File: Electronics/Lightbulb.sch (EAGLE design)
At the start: 22 parts, among them IC2 7805L

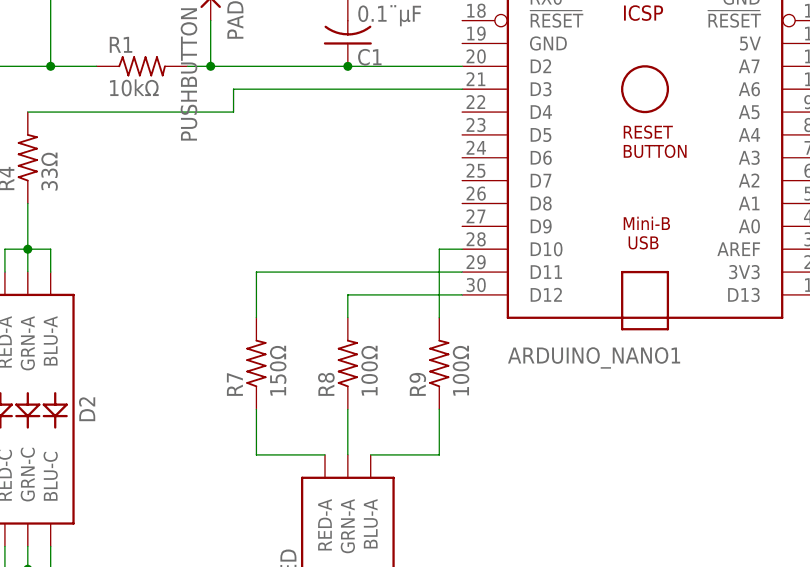
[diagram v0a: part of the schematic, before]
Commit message: Moving switches and LEDs to bottom side of board
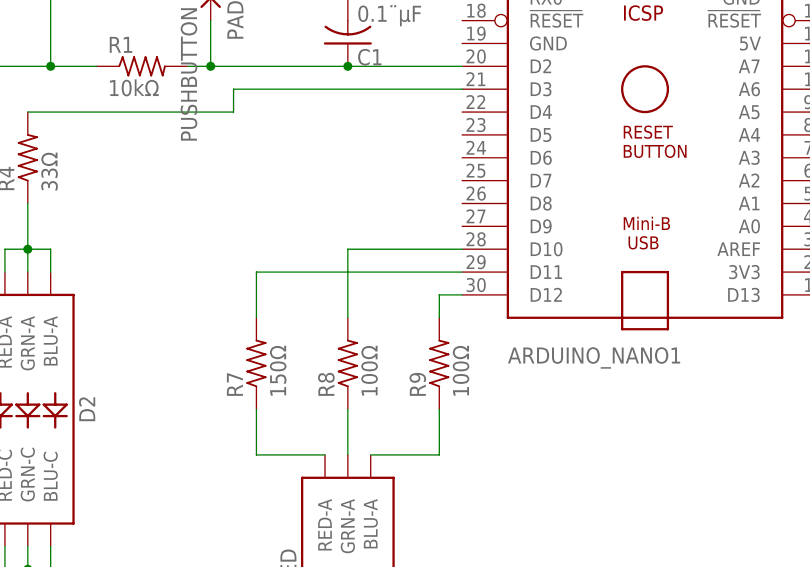
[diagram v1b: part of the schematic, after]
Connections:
- net N$12: now also ARDUINO_NANO1.D10; no longer ARDUINO_NANO1.D12
- net N$2: now also ARDUINO_NANO1.D12; no longer ARDUINO_NANO1.D10
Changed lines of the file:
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@@
-</segment>
-</net>
-<net name="N$2" class="0">
-<segment>
-<pinref part="R9" gate="G$1" pin="2"/>
-<wire x1="96.52" y1="58.42" x2="96.52" y2="66.04" width="0.1524" layer="91"/>
-<pinref part="ARDUINO_NANO1" gate="G$1" pin="D10"/>
-<wire x1="96.52" y1="66.04" x2="99.06" y2="66.04" width="0.1524" layer="91"/>
 </segment>
 </net>
@@
 </segment>
 </net>
-<net name="N$12" class="0">
-<segment>
-<pinref part="R8" gate="G$1" pin="2"/>
-<wire x1="86.36" y1="58.42" x2="86.36" y2="60.96" width="0.1524" layer="91"/>
-<pinref part="ARDUINO_NANO1" gate="G$1" pin="D12"/>
-<wire x1="86.36" y1="60.96" x2="99.06" y2="60.96" width="0.1524" layer="91"/>
-</segment>
-</net>
 <net name="N$1" class="0">
 <segment>
@@
 </segment>
 </net>
+<net name="N$2" class="0">
+<segment>
+<pinref part="ARDUINO_NANO1" gate="G$1" pin="D12"/>
+<wire x1="99.06" y1="60.96" x2="96.52" y2="60.96" width="0.1524" layer="91"/>
+<pinref part="R9" gate="G$1" pin="2"/>
+<wire x1="96.52" y1="60.96" x2="96.52" y2="58.42" width="0.1524" layer="91"/>
+</segment>
+</net>
+<net name="N$12" class="0">
+<segment>
+<pinref part="R8" gate="G$1" pin="2"/>
+<wire x1="86.36" y1="58.42" x2="86.36" y2="66.04" width="0.1524" layer="91"/>
+<pinref part="ARDUINO_NANO1" gate="G$1" pin="D10"/>
+<wire x1="86.36" y1="66.04" x2="99.06" y2="66.04" width="0.1524" layer="91"/>
+</segment>
+</net>

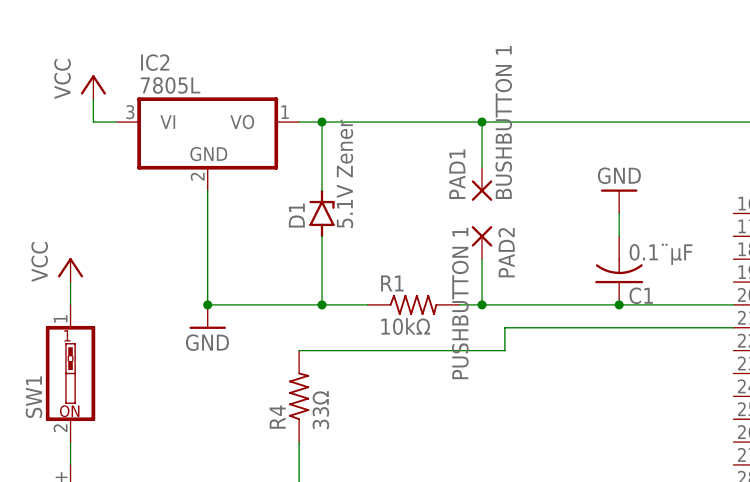
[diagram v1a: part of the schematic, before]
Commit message: Correcting pad placement and connections on PCB
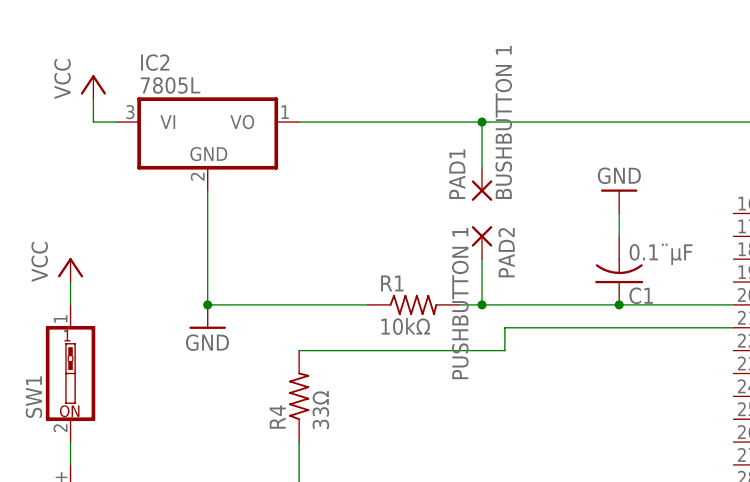
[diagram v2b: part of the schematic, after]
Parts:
- removed D1: 5.1V Zener, diode:ZENER-DIODESOD64-12
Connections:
- net GND: no longer D1.A
- net N$4: no longer D1.C
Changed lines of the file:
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@@
 <setting verticaltext="up"/>
 </settings>
-<grid distance="0.1" unitdist="inch" unit="inch" style="lines" multiple="1" display="yes" altdistance="0.01" altunitdist="inch" altunit="inch"/>
+<grid distance="0.1" unitdist="inch" unit="inch" style="lines" multiple="1" display="no" altdistance="0.01" altunitdist="inch" altunit="inch"/>
 <layers>
 <layer number="1" name="Top" color="4" fill="1" visible="no" active="no"/>
@@
 <part name="GND8" library="supply1" library_urn="urn:adsk.eagle:library:371" deviceset="GND" device=""/>
 <part name="D4" library="diode" library_urn="urn:adsk.eagle:library:210" deviceset="ZENER-DIODE" device="SOD64-12" package3d_urn="urn:adsk.eagle:package:43356/1" value="5.1V Zener"/>
-<part name="D1" library="diode" library_urn="urn:adsk.eagle:library:210" deviceset="ZENER-DIODE" device="SOD64-12" package3d_urn="urn:adsk.eagle:package:43356/1" value="5.1V Zener"/>
 <part name="D2" library="SparkFun-LED" library_urn="urn:adsk.eagle:library:529" deviceset="LED-RGB" device="NO_IC" package3d_urn="urn:adsk.eagle:package:39374/1" value="WHITE LED"/>
 <part name="P+2" library="supply1" library_urn="urn:adsk.eagle:library:371" deviceset="VCC" device=""/>
@@
 <attribute name="VALUE" x="176.149" y="59.182" size="1.778" layer="96" rot="R90"/>
 </instance>
-<instance part="D1" gate="G$1" x="53.34" y="96.52" rot="R90">
-<attribute name="NAME" x="51.435" y="94.742" size="1.778" layer="95" rot="R90"/>
-<attribute name="VALUE" x="56.769" y="94.742" size="1.778" layer="96" rot="R90"/>
-</instance>
 <instance part="D2" gate="G$1" x="50.8" y="48.26" rot="R270">
 <attribute name="NAME" x="56.515" y="48.26" size="1.778" layer="95" font="vector" rot="R270" align="bottom-center"/>
@@
 <net name="N$4" class="0">
 <segment>
-<wire x1="50.8" y1="106.68" x2="53.34" y2="106.68" width="0.1524" layer="91"/>
-<wire x1="53.34" y1="106.68" x2="71.12" y2="106.68" width="0.1524" layer="91"/>
+<wire x1="50.8" y1="106.68" x2="71.12" y2="106.68" width="0.1524" layer="91"/>
 <wire x1="71.12" y1="106.68" x2="71.12" y2="101.6" width="0.1524" layer="91"/>
 <wire x1="71.12" y1="106.68" x2="152.4" y2="106.68" width="0.1524" layer="91"/>
 <junction x="71.12" y="106.68"/>
 <wire x1="152.4" y1="106.68" x2="152.4" y2="88.9" width="0.1524" layer="91"/>
-<wire x1="53.34" y1="99.06" x2="53.34" y2="106.68" width="0.1524" layer="91"/>
-<junction x="53.34" y="106.68"/>
 <pinref part="ARDUINO_NANO1" gate="G$1" pin="5V"/>
 <wire x1="139.7" y1="88.9" x2="144.78" y2="88.9" width="0.1524" layer="91"/>
@@
 <wire x1="144.78" y1="86.36" x2="144.78" y2="88.9" width="0.1524" layer="91"/>
 <junction x="144.78" y="88.9"/>
-<pinref part="D1" gate="G$1" pin="C"/>
 <pinref part="IC2" gate="A1" pin="VO"/>
 <pinref part="PAD1" gate="G$1" pin="P"/>
@@
 <segment>
 <pinref part="R1" gate="G$1" pin="1"/>
-<wire x1="58.42" y1="86.36" x2="53.34" y2="86.36" width="0.1524" layer="91"/>
-<wire x1="53.34" y1="86.36" x2="40.64" y2="86.36" width="0.1524" layer="91"/>
+<wire x1="58.42" y1="86.36" x2="40.64" y2="86.36" width="0.1524" layer="91"/>
 <wire x1="40.64" y1="99.06" x2="40.64" y2="86.36" width="0.1524" layer="91"/>
-<wire x1="53.34" y1="93.98" x2="53.34" y2="86.36" width="0.1524" layer="91"/>
-<junction x="53.34" y="86.36"/>
-<pinref part="D1" gate="G$1" pin="A"/>
 <pinref part="GND9" gate="1" pin="GND"/>
 <junction x="40.64" y="86.36"/>

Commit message: Updating board with custom-made footprints for push buttons
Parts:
- removed PAD1: BUSHBUTTON 1, wirepad:WIREPADSMD1,27-254
- removed PAD2: PUSHBUTTON 1, wirepad:WIREPADSMD1,27-254
- removed PAD3: BUSHBUTTON 2, wirepad:WIREPADSMD1,27-254
- removed PAD4: PUSHBUTTON 2, wirepad:WIREPADSMD1,27-254
- added U$1, U$2: SKRPABE010, Custom Library:SKRPABE010
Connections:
- net N$3: now also U$1.3, U$1.4; no longer PAD2.P
- net N$4: now also U$1.1, U$1.2; no longer PAD1.P
- net N$6: now also U$2.3, U$2.4; no longer PAD4.P
- net VCC: now also U$2.1, U$2.2; no longer PAD3.P

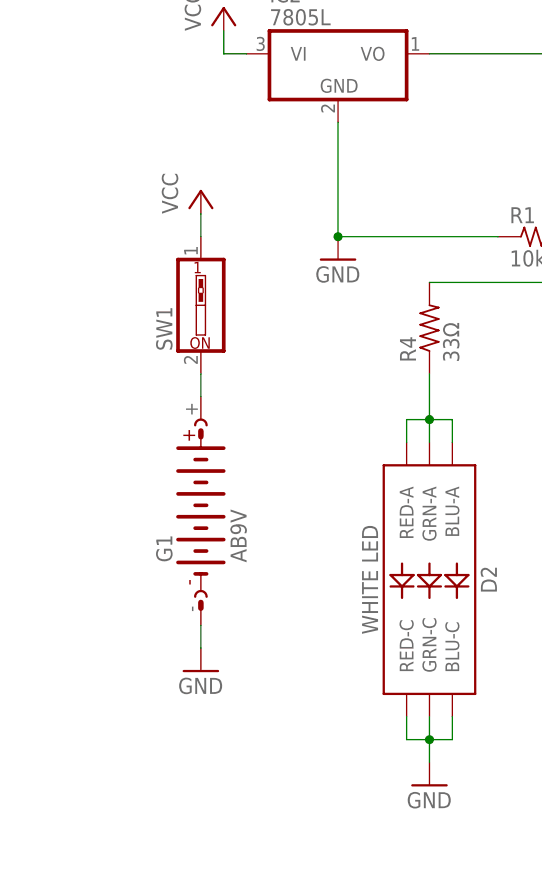
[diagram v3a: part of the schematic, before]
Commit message: Larger trace widths and new footprint for dip switch
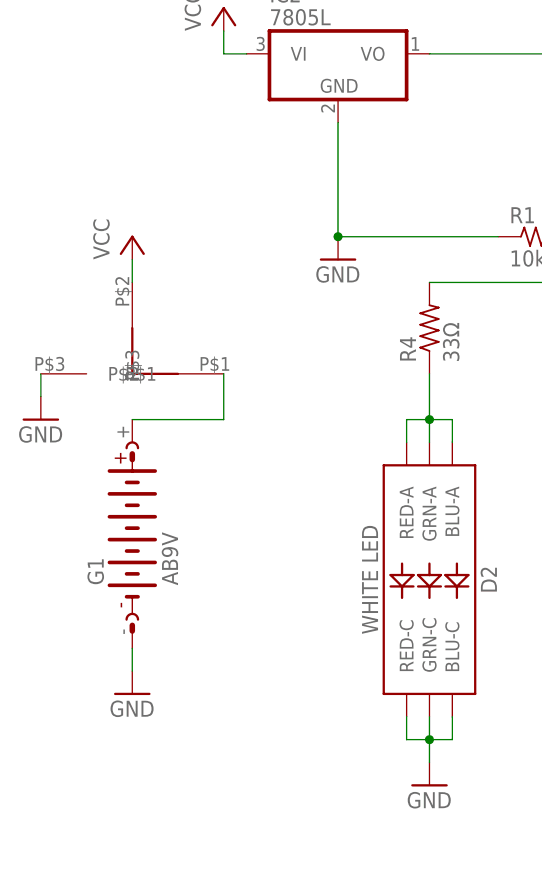
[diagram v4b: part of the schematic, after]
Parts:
- removed SW1: (no value), special:SW_DIP-1
- added U$3: DIPSWITCH, Custom Library:DIPSWITCH
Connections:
- net GND: now also U$3.P$2
- net N$1: now also U$3.P$1; no longer SW1.2
- net VCC: now also U$3.P$3; no longer SW1.1
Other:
- moved on the sheet: G1
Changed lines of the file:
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@@
 <setting verticaltext="up"/>
 </settings>
-<grid distance="0.1" unitdist="inch" unit="inch" style="lines" multiple="1" display="no" altdistance="0.01" altunitdist="mm" altunit="mm"/>
+<grid distance="0.1" unitdist="inch" unit="inch" style="lines" multiple="1" display="no" altdistance="0.01" altunitdist="inch" altunit="inch"/>
 <layers>
 <layer number="1" name="Top" color="4" fill="1" visible="yes" active="no"/>
@@
 </variantdefs>
 <classes>
-<class number="0" name="default" width="0.3048" drill="0.508">
+<class number="0" name="default" width="0.508" drill="0.508">
 <clearance class="0" value="0.3048"/>
 </class>
@@
 <part name="P+3" library="supply1" library_urn="urn:adsk.eagle:library:371" deviceset="VCC" device=""/>
 <part name="IC2" library="adafruit" deviceset="78*" device="L" technology="05"/>
-<part name="SW1" library="special" library_urn="urn:adsk.eagle:library:367" deviceset="SW_DIP-1" device="" package3d_urn="urn:adsk.eagle:package:26661/1"/>
 <part name="P+1" library="supply1" library_urn="urn:adsk.eagle:library:371" deviceset="VCC" device=""/>
 <part name="U$2" library="Custom Library" deviceset="SKRPABE010" device=""/>
 <part name="U$1" library="Custom Library" deviceset="SKRPABE010" device=""/>
+<part name="U$3" library="Custom Library" deviceset="DIPSWITCH" device=""/>
+<part name="GND10" library="supply1" library_urn="urn:adsk.eagle:library:371" deviceset="GND" device=""/>
 </parts>
 <sheets>
@@
 <attribute name="VALUE" x="145.796" y="79.629" size="1.778" layer="96"/>
 </instance>
-<instance part="G1" gate="G$1" x="25.4" y="55.88" rot="R90">
-<attribute name="NAME" x="22.225" y="50.165" size="1.778" layer="95" rot="R90"/>
-<attribute name="VALUE" x="30.48" y="50.165" size="1.778" layer="96" rot="R90"/>
+<instance part="G1" gate="G$1" x="17.78" y="53.34" rot="R90">
+<attribute name="NAME" x="14.605" y="47.625" size="1.778" layer="95" rot="R90"/>
+<attribute name="VALUE" x="22.86" y="47.625" size="1.778" layer="96" rot="R90"/>
 </instance>
 <instance part="GND1" gate="1" x="144.78" y="93.98" rot="R90">
 <attribute name="VALUE" x="147.32" y="91.44" size="1.778" layer="96" rot="R90"/>
 </instance>
-<instance part="GND2" gate="1" x="25.4" y="38.1">
-<attribute name="VALUE" x="22.86" y="35.56" size="1.778" layer="96"/>
+<instance part="GND2" gate="1" x="17.78" y="35.56">
+<attribute name="VALUE" x="15.24" y="33.02" size="1.778" layer="96"/>
 </instance>
 <instance part="ARDUINO_NANO1" gate="G$1" x="119.38" y="83.82">
@@
 <attribute name="VALUE" x="38.1" y="81.28" size="1.778" layer="96"/>
 </instance>
-<instance part="P+3" gate="VCC" x="25.4" y="91.44">
-<attribute name="VALUE" x="22.86" y="88.9" size="1.778" layer="96" rot="R90"/>
+<instance part="P+3" gate="VCC" x="17.78" y="86.36">
+<attribute name="VALUE" x="15.24" y="83.82" size="1.778" layer="96" rot="R90"/>
 </instance>
 <instance part="IC2" gate="A1" x="40.64" y="106.68">
@@
 <attribute name="VALUE" x="33.02" y="109.855" size="1.778" layer="96"/>
 </instance>
-<instance part="SW1" gate="G$1" x="25.4" y="78.74" rot="R90">
-<attribute name="NAME" x="22.225" y="73.66" size="1.778" layer="95" rot="R90"/>
-<attribute name="VALUE" x="30.48" y="73.66" size="1.778" layer="96" rot="R90"/>
-</instance>
 <instance part="P+1" gate="VCC" x="27.94" y="111.76">
 <attribute name="VALUE" x="25.4" y="109.22" size="1.778" layer="96" rot="R90"/>
@@
 <instance part="U$2" gate="G$1" x="165.1" y="99.06"/>
 <instance part="U$1" gate="G$1" x="76.2" y="101.6"/>
+<instance part="U$3" gate="G$1" x="17.78" y="71.12" rot="R180"/>
+<instance part="GND10" gate="1" x="7.62" y="66.04">
+<attribute name="VALUE" x="5.08" y="63.5" size="1.778" layer="96"/>
+</instance>
 </instances>
 <busses>
@@
 <pinref part="G1" gate="G$1" pin="-"/>
 <pinref part="GND2" gate="1" pin="GND"/>
-<wire x1="25.4" y1="40.64" x2="25.4" y2="43.18" width="0.1524" layer="91"/>
+<wire x1="17.78" y1="38.1" x2="17.78" y2="40.64" width="0.1524" layer="91"/>
 </segment>
 <segment>
@@
 <wire x1="88.9" y1="12.7" x2="88.9" y2="10.16" width="0.1524" layer="91"/>
 <wire x1="88.9" y1="10.16" x2="86.36" y2="10.16" width="0.1524" layer="91"/>
+</segment>
+<segment>
+<pinref part="U$3" gate="G$1" pin="P$2"/>
+<pinref part="GND10" gate="1" pin="GND"/>
+<wire x1="7.62" y1="68.58" x2="7.62" y2="71.12" width="0.1524" layer="91"/>
 </segment>
 </net>
@@
 </segment>
 <segment>
-<pinref part="SW1" gate="G$1" pin="1"/>
-<pinref part="P+3" gate="VCC" pin="VCC"/>
-<wire x1="25.4" y1="86.36" x2="25.4" y2="88.9" width="0.1524" layer="91"/>
-</segment>
-<segment>
 <pinref part="P+2" gate="VCC" pin="VCC"/>
 <wire x1="162.56" y1="106.68" x2="162.56" y2="104.14" width="0.1524" layer="91"/>
@@
 <wire x1="170.18" y1="99.06" x2="169.72" y2="99.06" width="0.1524" layer="91"/>
 </segment>
+<segment>
+<pinref part="U$3" gate="G$1" pin="P$3"/>
+<pinref part="P+3" gate="VCC" pin="VCC"/>
+<wire x1="17.78" y1="83.82" x2="17.78" y2="81.28" width="0.1524" layer="91"/>
+</segment>
 </net>
 <net name="N$8" class="0">
@@
 <pinref part="ARDUINO_NANO1" gate="G$1" pin="D11"/>
 <wire x1="76.2" y1="63.5" x2="99.06" y2="63.5" width="0.1524" layer="91"/>
-</segment>
-</net>
-<net name="N$1" class="0">
-<segment>
-<pinref part="G1" gate="G$1" pin="+"/>
-<pinref part="SW1" gate="G$1" pin="2"/>
-<wire x1="25.4" y1="68.58" x2="25.4" y2="71.12" width="0.1524" layer="91"/>
 </segment>
 </net>
@@
 </segment>
 </net>
+<net name="N$1" class="0">
+<segment>
+<pinref part="G1" gate="G$1" pin="+"/>
+<pinref part="U$3" gate="G$1" pin="P$1"/>
+<wire x1="17.78" y1="66.04" x2="27.94" y2="66.04" width="0.1524" layer="91"/>
+<wire x1="27.94" y1="66.04" x2="27.94" y2="71.12" width="0.1524" layer="91"/>
+</segment>
+</net>

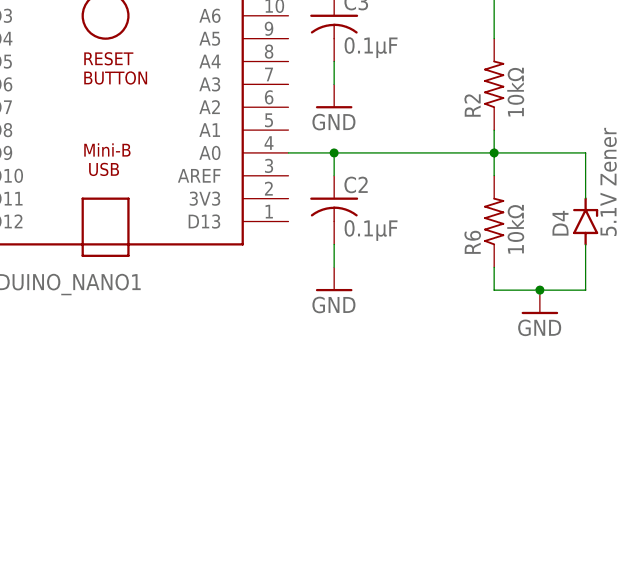
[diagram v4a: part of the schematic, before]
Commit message: Correct trace widths this time (Matt Brown approved)
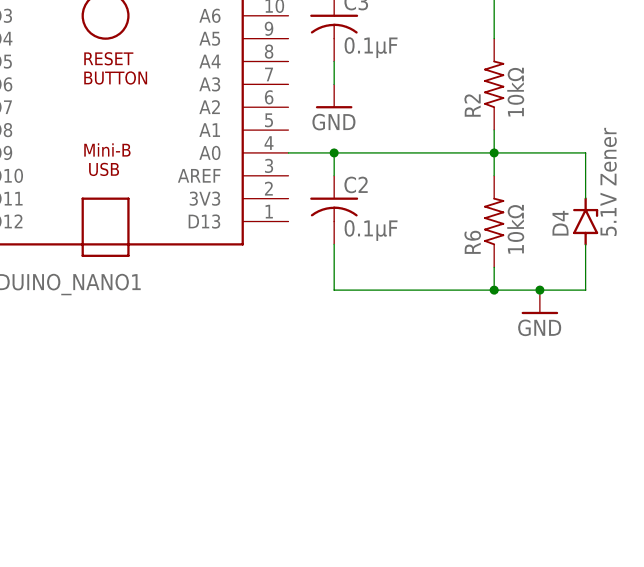
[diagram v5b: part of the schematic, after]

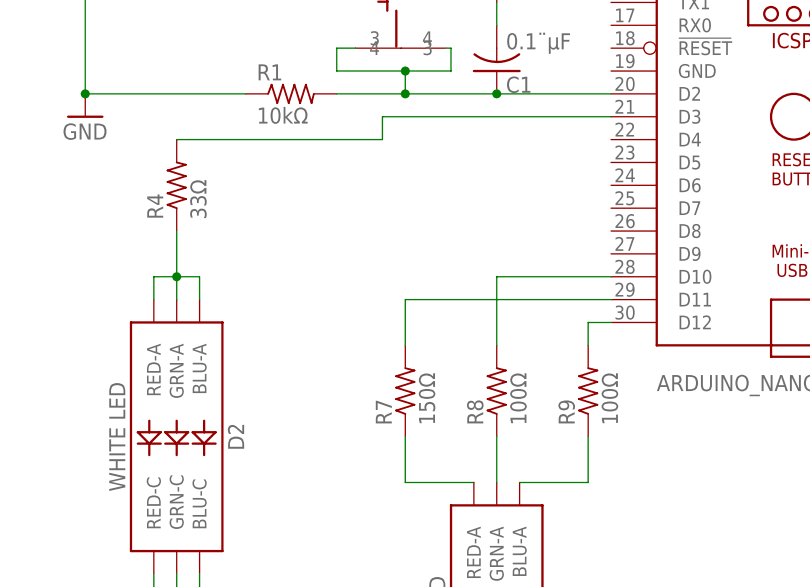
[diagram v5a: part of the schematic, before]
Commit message: updating a few resistor values for diodes to prevent draw of too much current from Arduino
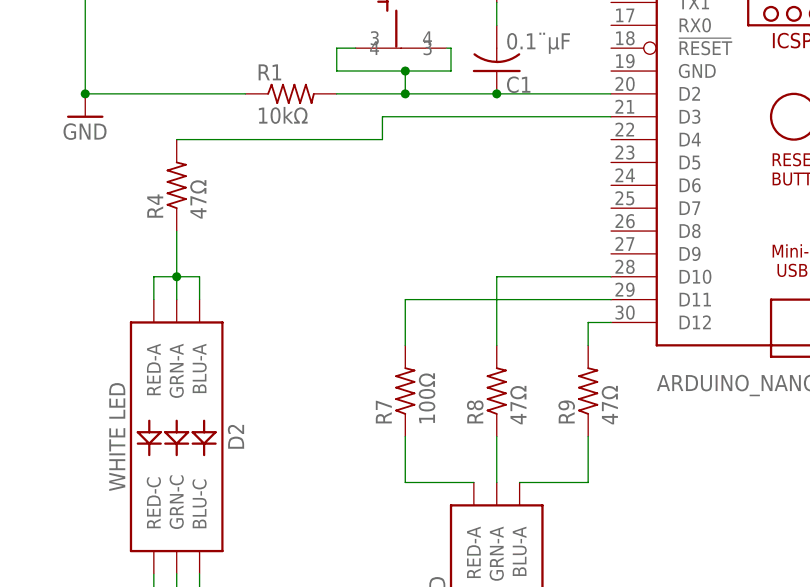
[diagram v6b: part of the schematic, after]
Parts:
- R4: value 33Ω -> 47Ω
- R7: value 150Ω -> 100Ω
- R8, R9: value 100Ω -> 47Ω
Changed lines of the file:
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@@
 <part name="R1" library="adafruit" deviceset="R-US_" device="R0805" value="10kΩ"/>
 <part name="R2" library="adafruit" deviceset="R-US_" device="R0805" value="10kΩ"/>
-<part name="R4" library="adafruit" deviceset="R-US_" device="R0805" value="33Ω"/>
+<part name="R4" library="adafruit" deviceset="R-US_" device="R0805" value="47Ω"/>
 <part name="R6" library="adafruit" deviceset="R-US_" device="R0805" value="10kΩ"/>
 <part name="C1" library="adafruit" deviceset="C-US" device="C0805" value="0.1¨µF"/>
@@
 <part name="GND7" library="supply1" library_urn="urn:adsk.eagle:library:371" deviceset="GND" device=""/>
 <part name="D3" library="SparkFun-LED" library_urn="urn:adsk.eagle:library:529" deviceset="LED-RGB" device="NO_IC" package3d_urn="urn:adsk.eagle:package:39374/1" value="RGB LED"/>
-<part name="R7" library="adafruit" deviceset="R-US_" device="R0805" value="150Ω"/>
-<part name="R8" library="adafruit" deviceset="R-US_" device="R0805" value="100Ω"/>
-<part name="R9" library="adafruit" deviceset="R-US_" device="R0805" value="100Ω"/>
+<part name="R7" library="adafruit" deviceset="R-US_" device="R0805" value="100Ω"/>
+<part name="R8" library="adafruit" deviceset="R-US_" device="R0805" value="47Ω"/>
+<part name="R9" library="adafruit" deviceset="R-US_" device="R0805" value="47Ω"/>
 <part name="GND8" library="supply1" library_urn="urn:adsk.eagle:library:371" deviceset="GND" device=""/>
 <part name="D4" library="diode" library_urn="urn:adsk.eagle:library:210" deviceset="ZENER-DIODE" device="SOD64-12" package3d_urn="urn:adsk.eagle:package:43356/1" value="5.1V Zener"/>
